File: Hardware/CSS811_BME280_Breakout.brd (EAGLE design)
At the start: 25.4 x 25.4 mm, 25 parts, among them J1 JST, J2 CCS811 Options, J3 JST, J4 PTH, U2 CCS811

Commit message: Initial Layout Finished - Ready for Review
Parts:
- moved FD1 5.12 mm to (1.27, 19.7)
- moved U$1 4.45 mm to (12.7, 23.5)
- moved U$2 4.45 mm to (12.7, 23.5)
- moved FD2 3.81 mm to (24.1, 1.27)
- moved C2 1.27 mm to (10.2, 16.5)
- moved R3 1.27 mm to (16.5, 16.5)
- moved R14 1.27 mm to (6.35, 8.89)
- moved R2 1.27 mm to (10.2, 6.35), turned to 0 degrees
- moved R4 1.27 mm to (16.5, 6.35)
- moved C1 1.27 mm to (16.5, 8.89), turned to 0 degrees
- moved ADR2 0.13 mm to (17.7, 12.7)
- turned R6 to 0 degrees
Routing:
- net 3.3V: track 0.00 -> 59.6 mm, vias 0 -> 7
- net SDA: track 0.00 -> 43.0 mm, vias 0 -> 4
- net SCL: track 0.00 -> 39.3 mm, vias 0 -> 2
- net !WAKE: track 0.00 -> 22.4 mm, vias 0 -> 2
- net !RST: track 0.00 -> 14.8 mm, vias 0 -> 1
- net !INT: track 0.00 -> 14.6 mm, vias 0 -> 2
- net SDO/ADR: track 0.00 -> 7.68 mm, vias 0 -> 2
- net CCS811_ADDR: track 0.00 -> 6.90 mm, vias 0 -> 1
- net N$4: track 0.00 -> 5.01 mm, vias 0 -> 1
- net N$5: track 0.00 -> 5.01 mm, vias 0 -> 1
- net NTC_SENSE: track 0.00 -> 0.60 mm
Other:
- board text added: "ADR2"

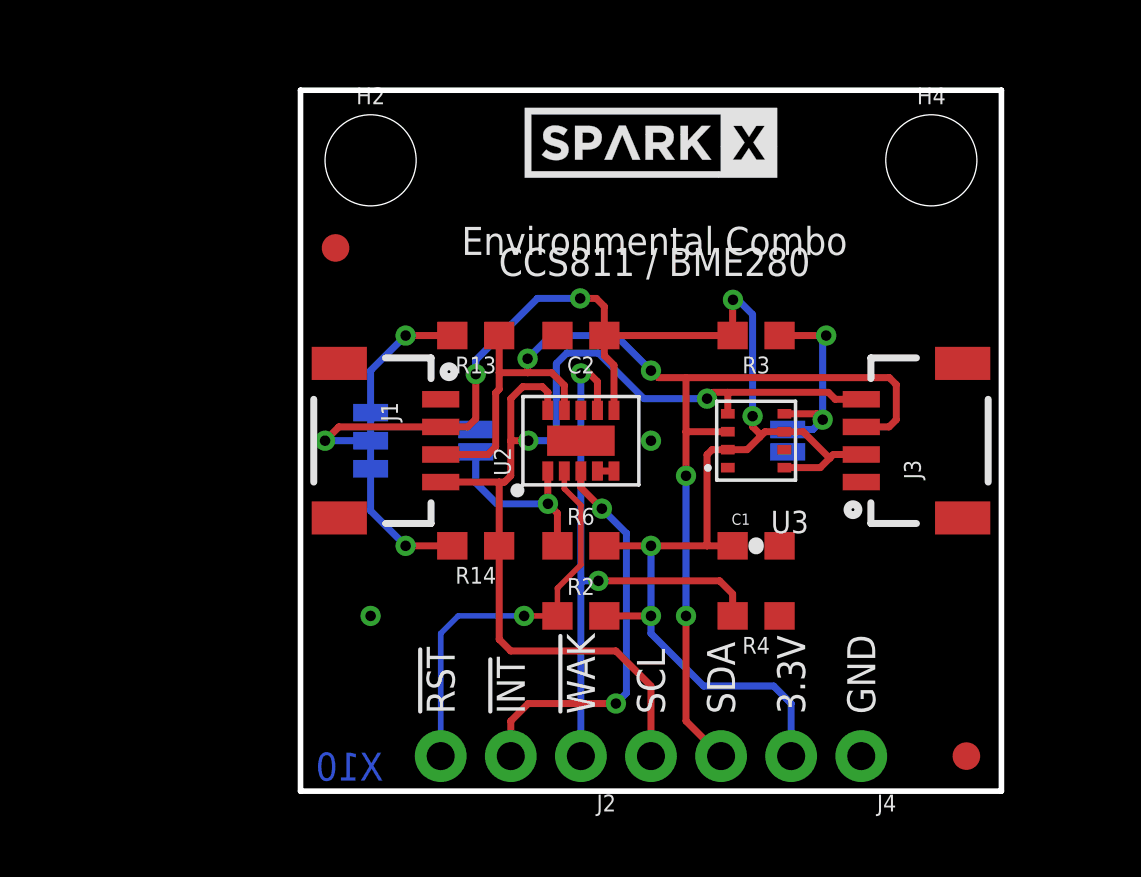
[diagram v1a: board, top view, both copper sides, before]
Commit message: Adjusted component to avoid silk.
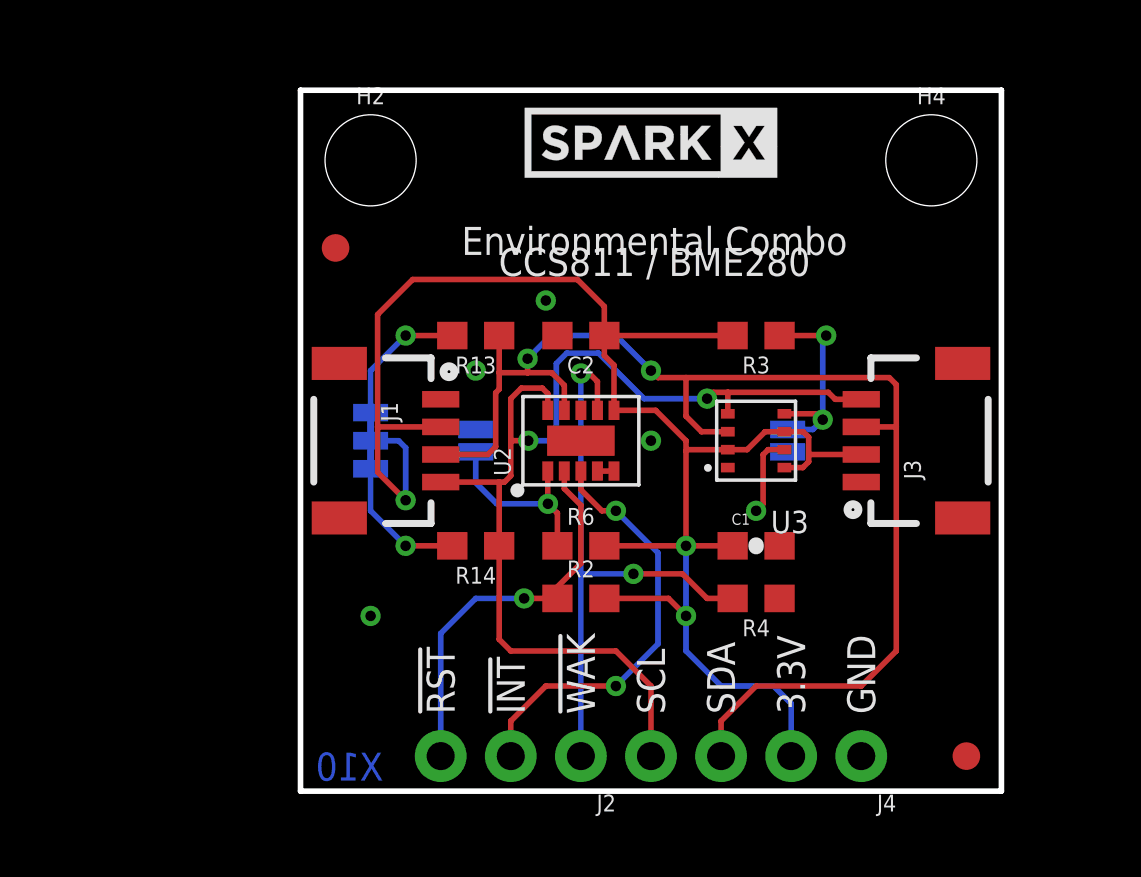
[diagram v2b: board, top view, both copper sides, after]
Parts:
- moved R2 0.64 mm to (10.2, 6.99)
- moved R4 0.64 mm to (16.5, 6.99)
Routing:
- net 3.3V: track 59.6 -> 64.1 mm, vias 7 -> 3
- net SDA: track 43.0 -> 47.3 mm, vias 4 -> 2
- net GND: track 0.00 -> 2.98 mm, vias 2 -> 5
- net !INT: track 14.6 -> 15.5 mm
- net !WAKE: track 22.4 -> 21.8 mm
